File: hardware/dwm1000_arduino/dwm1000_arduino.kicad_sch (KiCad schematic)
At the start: 0 parts

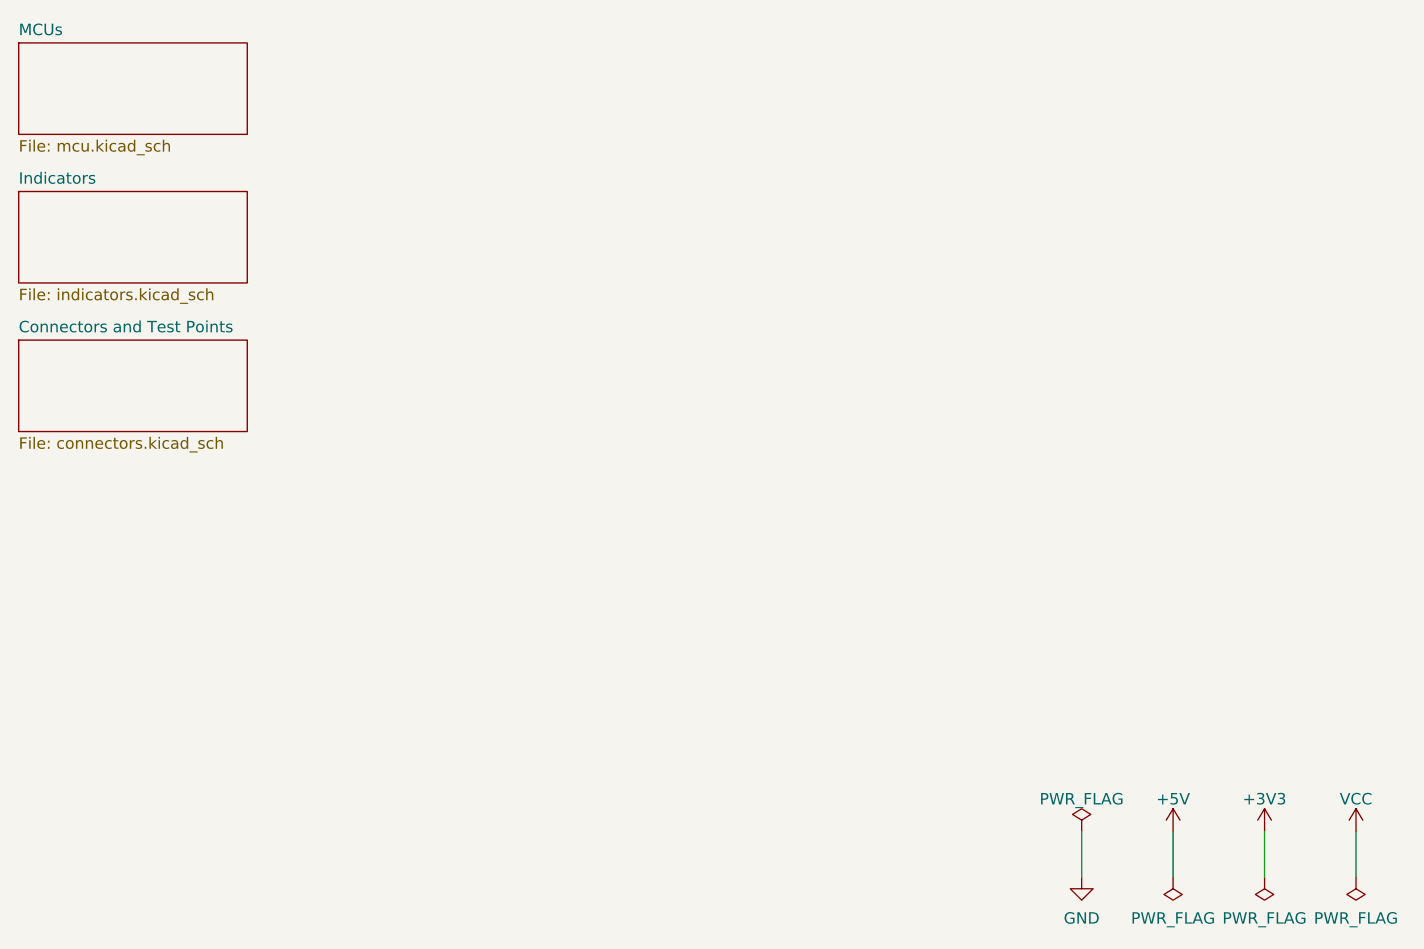
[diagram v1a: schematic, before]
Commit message: start rev 2 of the dwm board
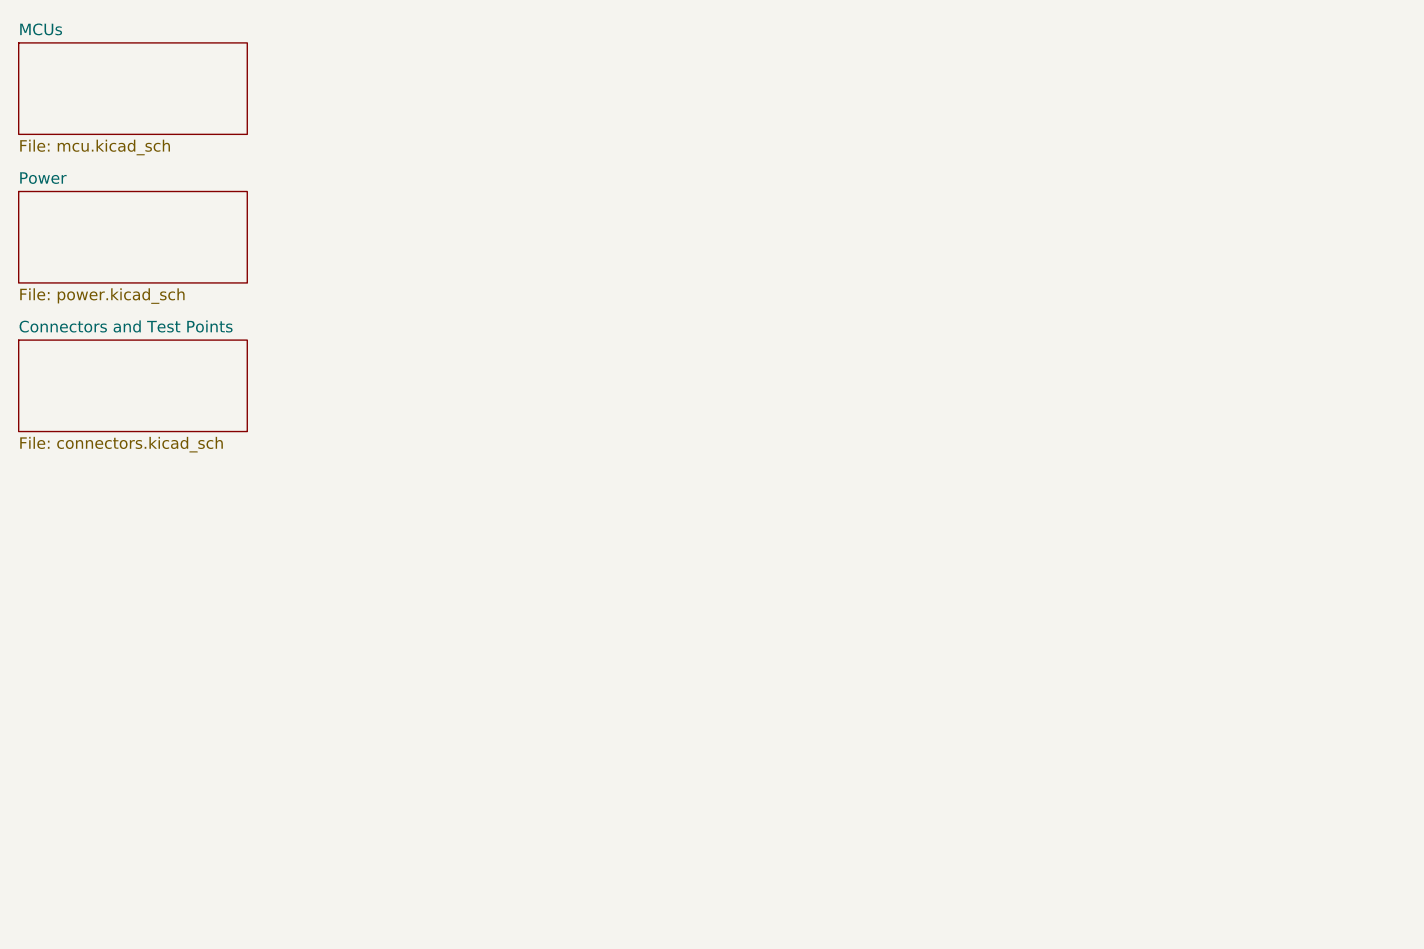
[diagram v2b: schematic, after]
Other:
- removed sheet Indicators
- added sheet Power (power.kicad_sch)

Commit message: finish layout
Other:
- title: DWM1000 Arduino Breakout -> DWM1000 AVR
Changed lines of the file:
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@@
   (paper "B")
   (title_block
-    (title "DWM1000 Arduino Breakout")
-    (date "2022-02-10")
-    (rev "A")
+    (title "DWM1000 AVR")
+    (date "2022-04-10")
+    (rev "B")
     (company "Olin Robotics - Project Firefly")
     (comment 1 "Designer: Wesley Soo-Hoo")
@@
       (reference "#PWR07") (unit 1) (value "GND") (footprint "")
     )
-    (path "/bbcfa2f2-5e07-498a-9f07-a4e9b06104d2/56bbc3de-e144-4293-9512-d91ad62fb4cf"
-      (reference "#PWR08") (unit 1) (value "GND") (footprint "")
-    )
     (path "/bbcfa2f2-5e07-498a-9f07-a4e9b06104d2/e3521387-aa85-4c30-9869-22e7fe603304"
       (reference "#PWR09") (unit 1) (value "+3V3") (footprint "")
@@
       (reference "#PWR012") (unit 1) (value "GND") (footprint "")
     )
-    (path "/bbcfa2f2-5e07-498a-9f07-a4e9b06104d2/77e7a046-ec8b-466e-b8b5-3d84e4ad1cf6"
-      (reference "#PWR013") (unit 1) (value "GND") (footprint "")
-    )
     (path "/bbcfa2f2-5e07-498a-9f07-a4e9b06104d2/335fe446-2ce4-495c-92db-4c7882b063f9"
       (reference "#PWR014") (unit 1) (value "+3V3") (footprint "")
@@
     )
     (path "/bbcfa2f2-5e07-498a-9f07-a4e9b06104d2/0a064f76-d938-4e21-95c2-a7ba7c24d066"
-      (reference "C1") (unit 1) (value "1uF") (footprint "")
+      (reference "C1") (unit 1) (value "1uF") (footprint "Capacitor_SMD:C_0805_2012Metric_Pad1.18x1.45mm_HandSolder")
     )
     (path "/bbcfa2f2-5e07-498a-9f07-a4e9b06104d2/58ff9996-d26b-4785-bb06-a0f9e1c440c2"
-      (reference "C2") (unit 1) (value "1uF") (footprint "")
+      (reference "C2") (unit 1) (value "1uF") (footprint "Capacitor_SMD:C_0805_2012Metric_Pad1.18x1.45mm_HandSolder")
     )
     (path "/bbcfa2f2-5e07-498a-9f07-a4e9b06104d2/385df312-20da-49e8-b054-b2a24defc785"
-      (reference "C3") (unit 1) (value "0.1uF") (footprint "")
+      (reference "C3") (unit 1) (value "0.1uF") (footprint "Capacitor_SMD:C_0805_2012Metric_Pad1.18x1.45mm_HandSolder")
     )
     (path "/bbcfa2f2-5e07-498a-9f07-a4e9b06104d2/3ba997e3-bd0c-4270-b008-3554a53e4437"
-      (reference "C4") (unit 1) (value "0.1uF") (footprint "")
+      (reference "C4") (unit 1) (value "0.1uF") (footprint "Capacitor_SMD:C_0805_2012Metric_Pad1.18x1.45mm_HandSolder")
     )
     (path "/bbcfa2f2-5e07-498a-9f07-a4e9b06104d2/ff6734c1-3f84-4fd4-9dc9-ba5773bff252"
-      (reference "C5") (unit 1) (value "0.1uF") (footprint "")
-    )
-    (path "/bbcfa2f2-5e07-498a-9f07-a4e9b06104d2/bd1535bb-c5f1-4965-8369-278cab9b60d8"
-      (reference "C6") (unit 1) (value "30pF") (footprint "")
-    )
-    (path "/bbcfa2f2-5e07-498a-9f07-a4e9b06104d2/9d72b5b8-28b8-4878-905d-491f1384e26b"
-      (reference "C7") (unit 1) (value "30pF") (footprint "")
+      (reference "C5") (unit 1) (value "0.1uF") (footprint "Capacitor_SMD:C_0805_2012Metric_Pad1.18x1.45mm_HandSolder")
     )
     (path "/bbcfa2f2-5e07-498a-9f07-a4e9b06104d2/c1543653-6a02-4236-9521-a35d29c00016"
-      (reference "C8") (unit 1) (value "1uF") (footprint "")
+      (reference "C8") (unit 1) (value "1uF") (footprint "Capacitor_SMD:C_0805_2012Metric_Pad1.18x1.45mm_HandSolder")
     )
     (path "/a1529949-083e-40ff-8a21-9e39b88171ef/7f188211-6c55-4668-97eb-072397d8eb6a"
-      (reference "C9") (unit 1) (value "1uF") (footprint "")
+      (reference "C9") (unit 1) (value "1uF") (footprint "Capacitor_SMD:C_0805_2012Metric_Pad1.18x1.45mm_HandSolder")
     )
     (path "/a1529949-083e-40ff-8a21-9e39b88171ef/66572e6e-6cc1-47f0-8cdb-b31a03ac1874"
-      (reference "C10") (unit 1) (value "1uF") (footprint "")
+      (reference "C10") (unit 1) (value "1uF") (footprint "Capacitor_SMD:C_0805_2012Metric_Pad1.18x1.45mm_HandSolder")
     )
     (path "/a1529949-083e-40ff-8a21-9e39b88171ef/b76c04b3-9a89-43e5-a52b-7f35224ec995"
-      (reference "C11") (unit 1) (value "1uF") (footprint "")
+      (reference "C11") (unit 1) (value "1uF") (footprint "Capacitor_SMD:C_0805_2012Metric_Pad1.18x1.45mm_HandSolder")
     )
     (path "/a1529949-083e-40ff-8a21-9e39b88171ef/50d06e10-075e-487d-b55a-8db7caffb4b2"
-      (reference "C12") (unit 1) (value "1uF") (footprint "")
+      (reference "C12") (unit 1) (value "1uF") (footprint "Capacitor_SMD:C_0805_2012Metric_Pad1.18x1.45mm_HandSolder")
     )
     (path "/a1529949-083e-40ff-8a21-9e39b88171ef/2f0d8e6a-7315-4999-b04c-a66c21fdc2f3"
-      (reference "C13") (unit 1) (value "4.7uF") (footprint "")
+      (reference "C13") (unit 1) (value "4.7uF") (footprint "Capacitor_SMD:C_0805_2012Metric_Pad1.18x1.45mm_HandSolder")
     )
     (path "/a1529949-083e-40ff-8a21-9e39b88171ef/f3c8f9f9-6608-415e-be62-509d8493cf52"
-      (reference "C14") (unit 1) (value "4.7uF") (footprint "")
+      (reference "C14") (unit 1) (value "4.7uF") (footprint "Capacitor_SMD:C_0805_2012Metric_Pad1.18x1.45mm_HandSolder")
     )
     (path "/5e06f65c-f2c6-4e90-84c8-a08a5998af78/c9c9e6e2-7f85-456e-b26c-35a3bad6b8eb"
@@
     )
     (path "/5e06f65c-f2c6-4e90-84c8-a08a5998af78/23d7699f-fd2c-426f-823e-c0a0d0840ba2"
-      (reference "J2") (unit 1) (value "PWR_IN") (footprint "TerminalBlock_Phoenix:TerminalBlock_Phoenix_PT-1,5-4-3.5-H_1x04_P3.50mm_Horizontal")
+      (reference "J2") (unit 1) (value "PWR_OUT") (footprint "TerminalBlock_Phoenix:TerminalBlock_Phoenix_PT-1,5-4-3.5-H_1x04_P3.50mm_Horizontal")
     )
     (path "/5e06f65c-f2c6-4e90-84c8-a08a5998af78/ec61ea89-14c7-4d5e-9d2b-609320d813ac"
-      (reference "J3") (unit 1) (value "AVR ICSP") (footprint "")
+      (reference "J3") (unit 1) (value "AVR ICSP") (footprint "Connector_PinHeader_2.54mm:PinHeader_2x03_P2.54mm_Vertical")
     )
     (path "/5e06f65c-f2c6-4e90-84c8-a08a5998af78/4f4cdfd0-3774-4e50-8f71-e083d7936ee5"
@@
     )
     (path "/bbcfa2f2-5e07-498a-9f07-a4e9b06104d2/6d9a38b4-8337-4e5e-be2c-43fa78bd6874"
-      (reference "R2") (unit 1) (value "10K") (footprint "")
+      (reference "R2") (unit 1) (value "10K") (footprint "Resistor_SMD:R_0805_2012Metric_Pad1.20x1.40mm_HandSolder")
     )
     (path "/bbcfa2f2-5e07-498a-9f07-a4e9b06104d2/2cc4b0b4-ab11-4116-aff3-5862f184ef88"
-      (reference "R3") (unit 1) (value "1K") (footprint "")
+      (reference "R3") (unit 1) (value "1K") (footprint "Resistor_SMD:R_0805_2012Metric_Pad1.20x1.40mm_HandSolder")
     )
     (path "/bbcfa2f2-5e07-498a-9f07-a4e9b06104d2/6dac8c3b-b607-4cc2-80bb-c929cc657f46"
-      (reference "R4") (unit 1) (value "1K") (footprint "")
+      (reference "R4") (unit 1) (value "1K") (footprint "Resistor_SMD:R_0805_2012Metric_Pad1.20x1.40mm_HandSolder")
     )
     (path "/bbcfa2f2-5e07-498a-9f07-a4e9b06104d2/21a40ef6-30e4-4ffb-bf7b-5752df939a18"
-      (reference "SW1") (unit 1) (value "RST") (footprint "")
+      (reference "SW1") (unit 1) (value "RST") (footprint "Button_Switch_THT:SW_PUSH_6mm")
     )
     (path "/5e06f65c-f2c6-4e90-84c8-a08a5998af78/f6ea1a3d-e490-4de5-ad2d-e7087b305217"
-      (reference "TP1") (unit 1) (value "5V") (footprint "TestPoint:TestPoint_Pad_D2.5mm")
+      (reference "TP1") (unit 1) (value "5V") (footprint "TestPoint:TestPoint_Pad_D1.0mm")
     )
     (path "/5e06f65c-f2c6-4e90-84c8-a08a5998af78/baa30378-08e9-4b99-80a4-c6b726f0f7a7"
-      (reference "TP2") (unit 1) (value "3V3") (footprint "TestPoint:TestPoint_Pad_D2.5mm")
-    )
-    (path "/bbcfa2f2-5e07-498a-9f07-a4e9b06104d2/43883f72-8378-4ec6-a2b3-8b2520529937"
-      (reference "TP3") (unit 1) (value "DWM_GPIO7") (footprint "")
-    )
-    (path "/bbcfa2f2-5e07-498a-9f07-a4e9b06104d2/7815305a-d604-4fe7-beb4-471721217511"
-      (reference "TP4") (unit 1) (value "DWM_GPIO4") (footprint "")
+      (reference "TP2") (unit 1) (value "3V3") (footprint "TestPoint:TestPoint_Pad_D1.0mm")
     )
     (path "/bbcfa2f2-5e07-498a-9f07-a4e9b06104d2/637c8028-648b-4638-a3f8-78719acb6687"
@@
       (reference "U3") (unit 1) (value "MIC5239-3.3YM") (footprint "Package_SO:SOIC-8_3.9x4.9mm_P1.27mm")
     )
-    (path "/bbcfa2f2-5e07-498a-9f07-a4e9b06104d2/f042a4d7-1372-4497-a09f-b108c908385a"
-      (reference "Y1") (unit 1) (value "Crystal_Small") (footprint "")
-    )
-  )
+  )
